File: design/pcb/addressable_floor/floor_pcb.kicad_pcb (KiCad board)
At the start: 2 copper layers, 75 x 222 mm, 41 parts, among them J1 Conn_01x10_Male, J10 shock_grid, J11 shock_grid, J2 Conn_01x10_Male, J3 DB25_Male, J4 shock_grid, J5 shock_grid, J6 shock_grid, J7 shock_grid, J8 shock_grid, J9 shock_grid

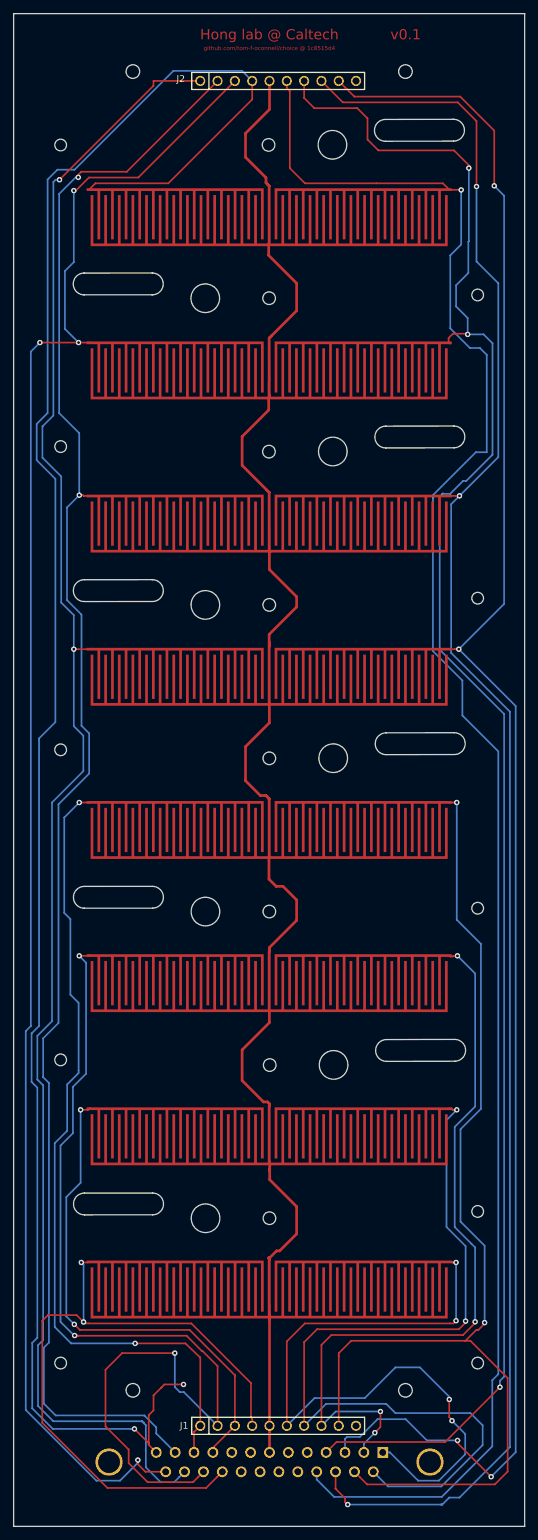
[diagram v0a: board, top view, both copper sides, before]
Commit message: Updated floor_pcb to Edge.Cuts repr of through holes, fixed trace that intersected one hole, and updated diam of outer holes to same 6-32 clearance. KiCAD df2819e crashing on zone fill attempt.
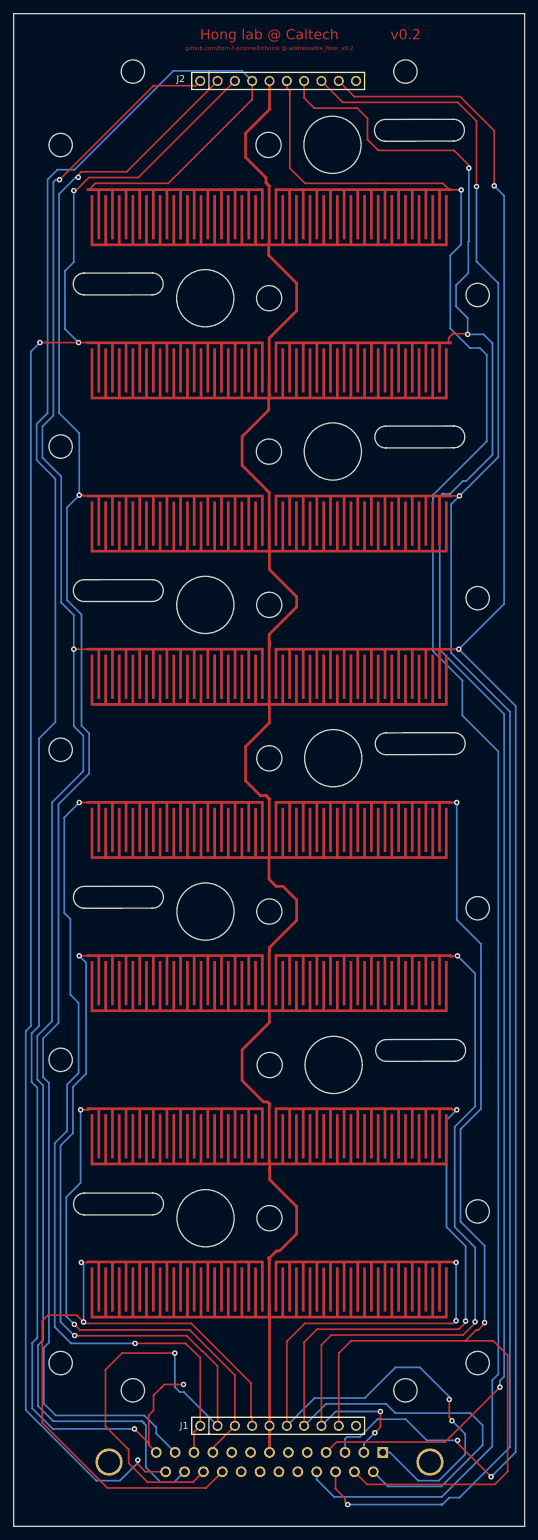
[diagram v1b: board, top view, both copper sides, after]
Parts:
- removed R1.7145mm_NPTH (x10): , R1.7145mm_NPTH
- removed R1.85178mm_NPTH (x8): , R1.85178mm_NPTH
- removed R2.0mm_NPTH (x4): , R2.0mm_NPTH
- removed R4.2mm_NPTH (x8): , R4.2mm_NPTH
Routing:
- net /F10: track 162.0 -> 164.0 mm
- net /F2: track 267.3 -> 266.3 mm
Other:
- outline, holes or cut-outs redrawn
- board text added: "Though the FR4 substrate for the current bottom acts as a diffuser for the IR backlights, substrates that transmit more IR are probably desirable. We have been using 850nm backlights."
- board text added: "github.com/tom-f-oconnell/choice @ addressable_floor_v0.2"
- board text added: "v0.2"
- board text removed: "Though the FR4 substrate for the current bottom acts as a diffuser for the IR backlights, substrates that transmit more IR are probably desirable. We should have been using 850nm backlights."
- board text removed: "github.com/tom-f-oconnell/choice @ 1c8515d4"
- board text removed: "v0.1"
